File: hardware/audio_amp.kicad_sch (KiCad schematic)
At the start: 9 parts, among them U8 OPA355NA

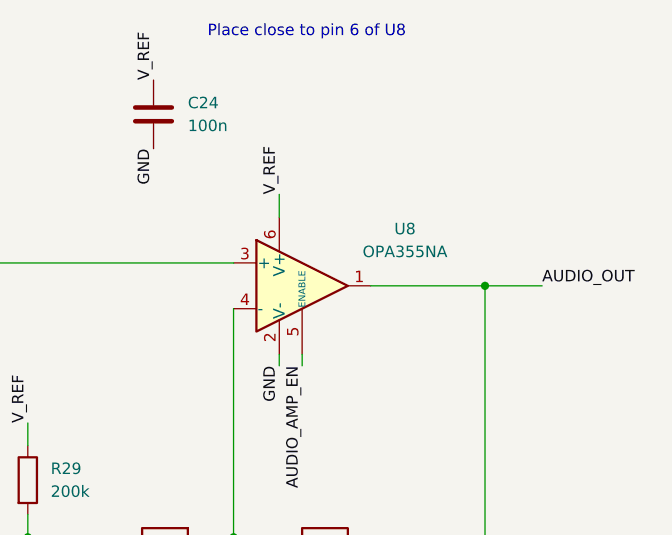
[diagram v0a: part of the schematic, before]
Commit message: [Hardware] Component changes.
* Swap op-amp to similar and cheaper OPA504
* Remove note about tantalum caps (per conversation w Alexa) and plan to replace in BOM with ceramic
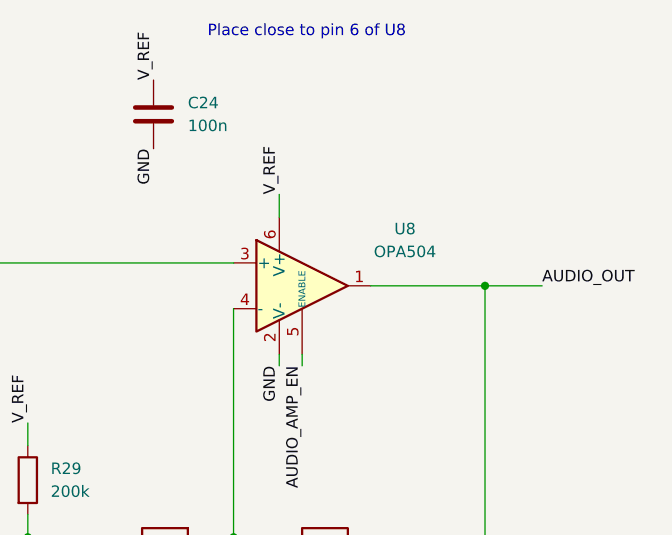
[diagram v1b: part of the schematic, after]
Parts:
- U8: value OPA355NA -> OPA504; symbol Amplifier_Operational:OPA355NA -> holiday-widget:OPA504
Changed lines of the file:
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@@
 	)
 	(symbol
-		(lib_id "Amplifier_Operational:OPA355NA")
+		(lib_id "holiday-widget:OPA504")
 		(at 179.07 85.09 0)
 		(unit 1)
@@
 			)
 		)
-		(property "Value" "OPA355NA"
+		(property "Value" "OPA504"
 			(at 190.5 81.3114 0)
 			(effects
@@
 			)
 		)
-		(property "Datasheet" "http://www.ti.com/lit/ds/symlink/opa355.pdf"
+		(property "Datasheet" "https://wmsc.lcsc.com/wmsc/upload/file/pdf/v2/lcsc/2303080930_analogysemi-OPA504ASOT236_C5349830.pdf"
 			(at 182.88 81.28 0)
 			(effects
@@
 			)
 		)
-		(property "Description" "200MHz, CMOS, Operational amplifier, with shutdown, SOT-23-6"
+		(property "Description" "5V, High-Precision, Ultra-Low-Power Operational Amplifiers"
 			(at 179.07 85.09 0)
 			(effects

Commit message: Change many passives to 0402 and assign part numbers
Incorporate 0402 parts where possible
Assign Manufacturer Part Numbers to parts where possible
Update layout for the new passive sizes
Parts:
- C22: MPN (none) -> CL10A106MQ8NNNC
- C24: footprint Capacitor_SMD:C_0603_1608Metric_Pad1.08x0.95mm_HandSolder -> Capacitor_SMD:C_0402_1005Metric; MPN (none) -> CL05A104KA5NNNC
- R27, R28, R29, R30: footprint Resistor_SMD:R_0603_1608Metric_Pad0.98x0.95mm_HandSolder -> Resistor_SMD:R_0402_1005Metric; MPN (none) -> RC0402FR-07200KL
- R31: footprint Resistor_SMD:R_0603_1608Metric_Pad0.98x0.95mm_HandSolder -> Resistor_SMD:R_0402_1005Metric; MPN (none) -> RC0402FR-07100KL
- R32: footprint Resistor_SMD:R_0603_1608Metric_Pad0.98x0.95mm_HandSolder -> Resistor_SMD:R_0402_1005Metric; MPN (none) -> RC0402JR-071M8L
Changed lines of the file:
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@@
 			)
 		)
-		(property "Footprint" "Resistor_SMD:R_0603_1608Metric_Pad0.98x0.95mm_HandSolder"
+		(property "Footprint" "Resistor_SMD:R_0402_1005Metric"
 			(at 181.61 114.808 90)
 			(effects
@@
 		)
 		(property "Description" "Resistor"
+			(at 181.61 113.03 0)
+			(effects
+				(font
+					(size 1.27 1.27)
+				)
+				(hide yes)
+			)
+		)
+		(property "MPN" "RC0402JR-071M8L"
 			(at 181.61 113.03 0)
 			(effects
@@
 			)
 		)
-		(property "Footprint" "Resistor_SMD:R_0603_1608Metric_Pad0.98x0.95mm_HandSolder"
+		(property "Footprint" "Resistor_SMD:R_0402_1005Metric"
 			(at 123.952 91.44 90)
 			(effects
@@
 		)
 		(property "Description" "Resistor"
+			(at 125.73 91.44 0)
+			(effects
+				(font
+					(size 1.27 1.27)
+				)
+				(hide yes)
+			)
+		)
+		(property "MPN" "RC0402FR-07200KL"
 			(at 125.73 91.44 0)
 			(effects
@@
 			)
 		)
-		(property "Footprint" "Resistor_SMD:R_0603_1608Metric_Pad0.98x0.95mm_HandSolder"
+		(property "Footprint" "Resistor_SMD:R_0402_1005Metric"
 			(at 146.812 106.68 90)
 			(effects
@@
 		)
 		(property "Description" "Resistor"
+			(at 148.59 106.68 0)
+			(effects
+				(font
+					(size 1.27 1.27)
+				)
+				(hide yes)
+			)
+		)
+		(property "MPN" "RC0402FR-07200KL"
 			(at 148.59 106.68 0)
 			(effects
@@
 			)
 		)
-		(property "Footprint" "Capacitor_SMD:C_0603_1608Metric_Pad1.08x0.95mm_HandSolder"
+		(property "Footprint" "Capacitor_SMD:C_0402_1005Metric"
 			(at 161.5948 62.23 0)
 			(effects
@@
 		)
 		(property "Description" "Unpolarized capacitor"
+			(at 162.56 66.04 0)
+			(effects
+				(font
+					(size 1.27 1.27)
+				)
+				(hide yes)
+			)
+		)
+		(property "MPN" "CL05A104KA5NNNC"
 			(at 162.56 66.04 0)
 			(effects
@@
 			)
 		)
-		(property "Footprint" "Resistor_SMD:R_0603_1608Metric_Pad0.98x0.95mm_HandSolder"
+		(property "Footprint" "Resistor_SMD:R_0402_1005Metric"
 			(at 146.812 118.11 90)
 			(effects
@@
 		)
 		(property "Description" "Resistor"
+			(at 148.59 118.11 0)
+			(effects
+				(font
+					(size 1.27 1.27)
+				)
+				(hide yes)
+			)
+		)
+		(property "MPN" "RC0402FR-07200KL"
 			(at 148.59 118.11 0)
 			(effects
@@
 			)
 		)
-		(property "Footprint" "Resistor_SMD:R_0603_1608Metric_Pad0.98x0.95mm_HandSolder"
+		(property "Footprint" "Resistor_SMD:R_0402_1005Metric"
 			(at 123.952 74.93 90)
 			(effects
@@
 		)
 		(property "Description" "Resistor"
+			(at 125.73 74.93 0)
+			(effects
+				(font
+					(size 1.27 1.27)
+				)
+				(hide yes)
+			)
+		)
+		(property "MPN" "RC0402FR-07200KL"
 			(at 125.73 74.93 0)
 			(effects
@@
 			)
 		)
-		(property "Footprint" "Resistor_SMD:R_0603_1608Metric_Pad0.98x0.95mm_HandSolder"
+		(property "Footprint" "Resistor_SMD:R_0402_1005Metric"
 			(at 163.83 111.252 90)
 			(effects
@@
 		)
 		(property "Description" "Resistor"
+			(at 163.83 113.03 0)
+			(effects
+				(font
+					(size 1.27 1.27)
+				)
+				(hide yes)
+			)
+		)
+		(property "MPN" "RC0402FR-07100KL"
 			(at 163.83 113.03 0)
 			(effects
@@
 			)
 		)
+		(property "MPN" "CL10A106MQ8NNNC"
+			(at 118.11 82.55 0)
+			(effects
+				(font
+					(size 1.27 1.27)
+				)
+				(hide yes)
+			)
+		)
 		(pin "2"
 		)
@@
 			(at 179.07 85.09 0)
 			(effects
+				(font
+					(size 1.27 1.27)
+				)
+				(hide yes)
+			)
+		)
+		(property "MPN" ""
+			(at 179.07 85.09 0)
+			(effects
